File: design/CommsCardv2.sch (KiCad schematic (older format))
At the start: 0 parts

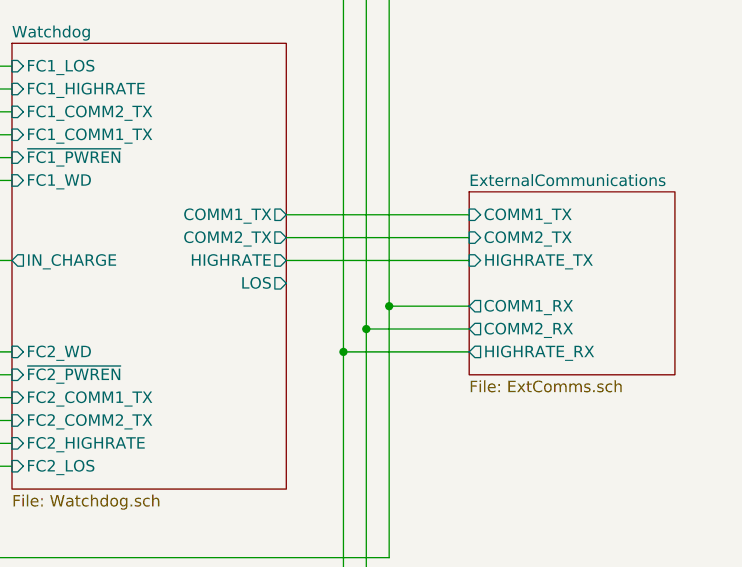
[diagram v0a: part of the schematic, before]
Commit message: Adding missing LOS wire
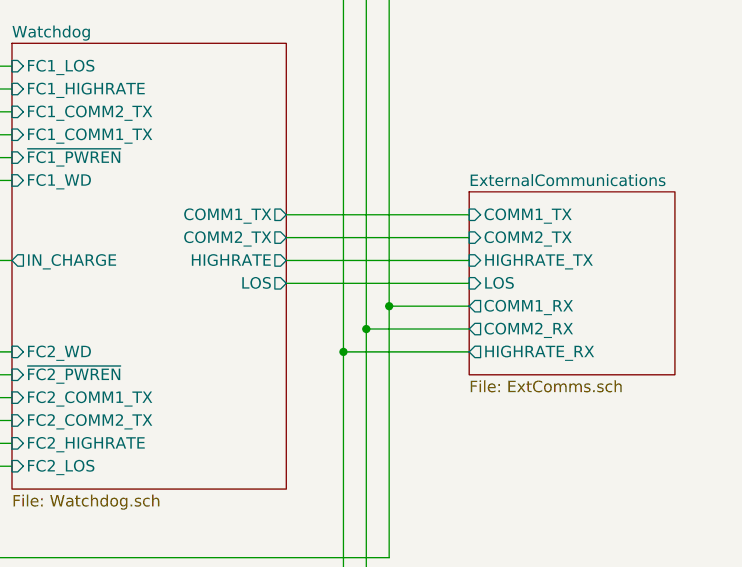
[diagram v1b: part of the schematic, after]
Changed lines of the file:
@@
 F6 "COMM2_RX" O L 8250 4450 50
 F7 "HIGHRATE_RX" O L 8250 4550 50
+F8 "LOS" I L 8250 4250 50
 $EndSheet
 $Sheet
@@
 Wire Wire Line
 	5100 2750 7700 2750
+Wire Wire Line
+	8250 4250 7450 4250
 $EndSCHEMATC

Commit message: Finished ERC
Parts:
- added NT101: NP, NetTie:NetTie-3_SMD_Pad2.0mm, symbol Device:Net-Tie_3_Tee
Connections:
- new net GND: NT101.3
- new net GNDPWR: NT101.1
- new net GNDS: NT101.2
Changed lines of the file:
@@
 $Descr A4 11693 8268
 encoding utf-8
-Sheet 1 8
+Sheet 1 10
 Title ""
 Date ""
@@
 $EndDescr
 $Sheet
-S 2000 950  1450 850
+S 2500 1100 1450 850
 U 5A78E52F
 F0 "Power" 50
@@
 Wire Wire Line
 	8250 4250 7450 4250
+$Comp
+L Device:Net-Tie_3_Tee NT101
+U 1 1 5A8BA840
+P 9800 1400
+F 0 "NT101" H 9800 1486 50  0000 C CNN
+F 1 "NP" H 9800 1487 50  0001 C CNN
+F 2 "NetTie:NetTie-3_SMD_Pad2.0mm" H 9800 1400 50  0001 C CNN
+F 3 "~" H 9800 1400 50  0001 C CNN
+	1    9800 1400
+	1    0    0    -1
+$EndComp
+$Comp
+L power:GND #PWR0102
+U 1 1 5A8BA88C
+P 9800 1500
+F 0 "#PWR0102" H 9800 1250 50  0001 C CNN
+F 1 "GND" H 9805 1327 50  0000 C CNN
+F 2 "" H 9800 1500 50  0001 C CNN
+F 3 "" H 9800 1500 50  0001 C CNN
+	1    9800 1500
+	1    0    0    -1
+$EndComp
+$Comp
+L power:GNDS #PWR0103
+U 1 1 5A8BA926
+P 10050 1450
+F 0 "#PWR0103" H 10050 1200 50  0001 C CNN
+F 1 "GNDS" H 10055 1277 50  0000 C CNN
+F 2 "" H 10050 1450 50  0001 C CNN
+F 3 "" H 10050 1450 50  0001 C CNN
+	1    10050 1450
+	1    0    0    -1
+$EndComp
+Wire Wire Line
+	10050 1450 10050 1400
+Wire Wire Line
+	10050 1400 9900 1400
+$Comp
+L power:GNDPWR #PWR0101
+U 1 1 5A8BB0D4
+P 9550 1500
+F 0 "#PWR0101" H 9550 1300 50  0001 C CNN
+F 1 "GNDPWR" H 9554 1574 50  0000 C CNN
+F 2 "" H 9550 1450 50  0001 C CNN
+F 3 "" H 9550 1450 50  0001 C CNN
+	1    9550 1500
+	1    0    0    -1
+$EndComp
+Wire Wire Line
+	9550 1500 9550 1400
+Wire Wire Line
+	9550 1400 9700 1400
+$Comp
+L power:PWR_FLAG #FLG0102
+U 1 1 5A8BBC47
+P 10050 1400
+F 0 "#FLG0102" H 10050 1475 50  0001 C CNN
+F 1 "PWR_FLAG" H 10050 1574 50  0000 C CNN
+F 2 "" H 10050 1400 50  0001 C CNN
+F 3 "" H 10050 1400 50  0001 C CNN
+	1    10050 1400
+	1    0    0    -1
+$EndComp
+Connection ~ 10050 1400
+$Comp
+L power:PWR_FLAG #FLG0101
+U 1 1 5A8BBC5B
+P 9550 1400
+F 0 "#FLG0101" H 9550 1475 50  0001 C CNN
+F 1 "PWR_FLAG" H 9550 1574 50  0000 C CNN
+F 2 "" H 9550 1400 50  0001 C CNN
+F 3 "" H 9550 1400 50  0001 C CNN
+	1    9550 1400
+	1    0    0    -1
+$EndComp
+Connection ~ 9550 1400
+$Sheet
+S 2500 2600 1000 1450
+U 5A8C396A
+F0 "FC1_USB" 50
+F1 "USB.sch" 50
+F2 "USB_DP" B R 3500 3450 50
+F3 "USB_DM" B R 3500 3350 50
+$EndSheet
+Wire Wire Line
+	3500 3450 3800 3450
+Wire Wire Line
+	3800 3350 3500 3350
+$Sheet
+S 2500 4300 1000 1450
+U 5A8D14B5
+F0 "FC2_USB" 50
+F1 "USB.sch" 50
+F2 "USB_DP" B R 3500 5150 50
+F3 "USB_DM" B R 3500 5050 50
+$EndSheet
+Wire Wire Line
+	3500 5050 3800 5050
+Wire Wire Line
+	3800 5150 3500 5150
 $EndSCHEMATC
